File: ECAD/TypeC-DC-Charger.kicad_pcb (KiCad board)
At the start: 4 copper layers, 48 x 56 mm, 97 parts, among them CON1 XT60-PT-MALE, J1 USB_C_SOCKET_RA_SMD, Q1 CSD18543Q3A, Q2 CSD18543Q3A, Q3 CSD17551Q3A, Q4 CSD17551Q3A, Q5 CSD17579Q3A, Q6 CSD17579Q3A, Q7 CSD17579Q3A, Q8 BC857B, Q9 IRFR9024NTRPBF, SW1 2.54mm_3xSPST_SMD, U1 LM5175RHF, U2 TPS25741, U3 TPS2514

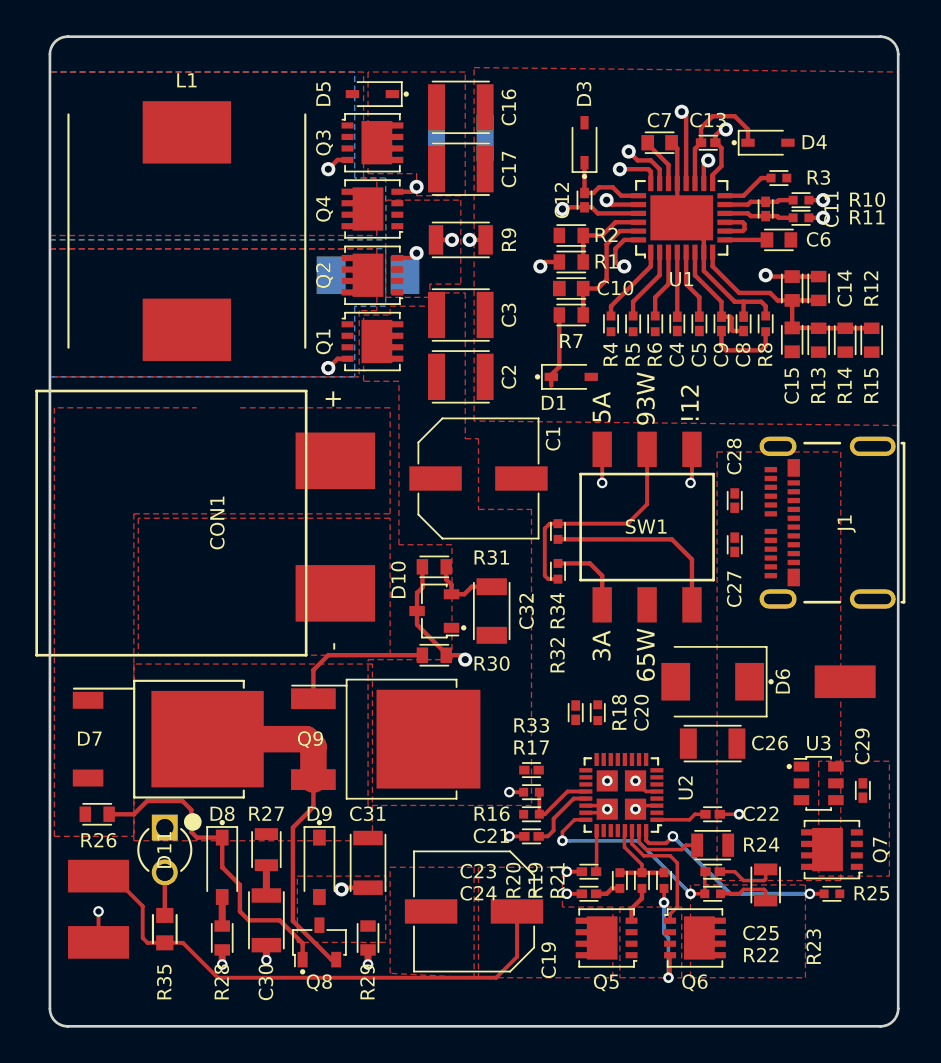
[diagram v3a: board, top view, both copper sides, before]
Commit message: Adding vias on thermal planes
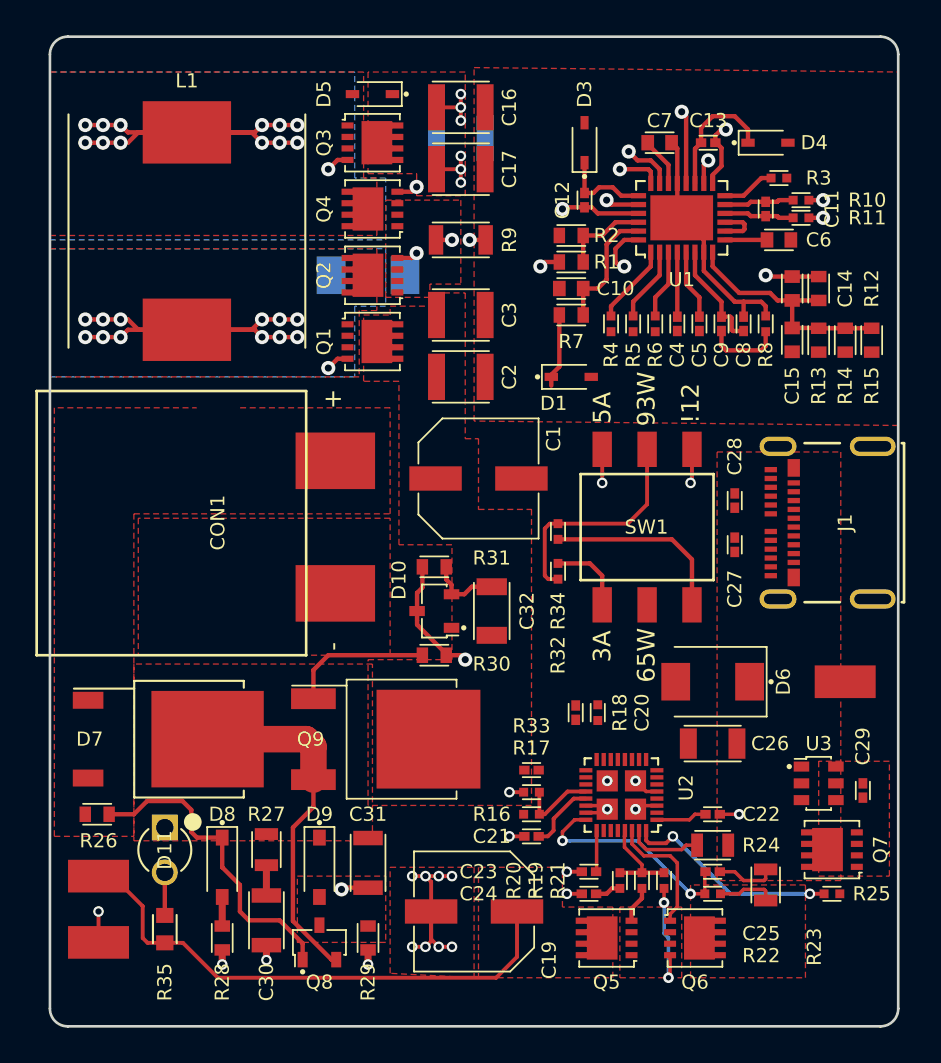
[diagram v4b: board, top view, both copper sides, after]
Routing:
- net SW2: track 3.82 -> 28.7 mm, vias 1 -> 13
- net SW1: track 4.49 -> 29.3 mm, vias 1 -> 13
- net GND: track 33.3 -> 43.5 mm, vias 17 -> 25
- net VARIABLE_DC: track 40.9 -> 46.6 mm, vias 2 -> 8
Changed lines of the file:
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@@
     (thickness 1)
     (drawings 15)
-    (tracks 353)
+    (tracks 442)
     (zones 0)
     (modules 97)
@@
   (segment (start 136.75 64.75) (end 136.75 65.845) (width 0.25) (layer F.Cu) (net 10))
   (segment (start 136 62.195) (end 136 64) (width 0.25) (layer F.Cu) (net 10))
+  (segment (start 123.25 54) (end 123.25 54.75) (width 0.22) (layer F.Cu) (net 11))
+  (via (at 123.25 54.75) (size 0.6) (drill 0.35) (layers F.Cu B.Cu) (net 11))
+  (segment (start 123.25 54) (end 123.25 53.25) (width 0.22) (layer F.Cu) (net 11))
+  (via (at 123.25 53.25) (size 0.6) (drill 0.35) (layers F.Cu B.Cu) (net 11))
+  (segment (start 121.875 54) (end 123.25 54) (width 0.22) (layer F.Cu) (net 11))
+  (via (at 123.25 54) (size 0.6) (drill 0.35) (layers F.Cu B.Cu) (net 11))
+  (segment (start 123.25 57.5) (end 123.25 56.75) (width 0.22) (layer F.Cu) (net 11))
+  (via (at 123.25 56.75) (size 0.6) (drill 0.35) (layers F.Cu B.Cu) (net 11))
+  (segment (start 123.25 57.5) (end 123.25 58.25) (width 0.22) (layer F.Cu) (net 11))
+  (via (at 123.25 58.25) (size 0.6) (drill 0.35) (layers F.Cu B.Cu) (net 11))
+  (segment (start 121.875 57.5) (end 123.25 57.5) (width 0.22) (layer F.Cu) (net 11))
+  (via (at 123.25 57.5) (size 0.6) (drill 0.35) (layers F.Cu B.Cu) (net 11))
   (segment (start 106.5 101.275) (end 107.525 101.275) (width 0.22) (layer F.Cu) (net 11))
   (segment (start 107.525 101.275) (end 109.5 103.25) (width 0.22) (layer F.Cu) (net 11))
@@
   (segment (start 136.5 58.305) (end 136.5 56.345) (width 0.25) (layer F.Cu) (net 18))
   (segment (start 136.5 56.345) (end 136.845 56) (width 0.25) (layer F.Cu) (net 18))
+  (segment (start 113 56) (end 114 56) (width 0.25) (layer F.Cu) (net 19))
+  (via (at 114 56) (size 0.8) (drill 0.4) (layers F.Cu B.Cu) (net 19))
+  (segment (start 112 56) (end 113 56) (width 0.25) (layer F.Cu) (net 19))
+  (via (at 113 56) (size 0.8) (drill 0.4) (layers F.Cu B.Cu) (net 19))
+  (segment (start 107.75 55.415) (end 111.415 55.415) (width 0.25) (layer F.Cu) (net 19))
+  (segment (start 111.415 55.415) (end 112 56) (width 0.25) (layer F.Cu) (net 19))
+  (via (at 112 56) (size 0.8) (drill 0.4) (layers F.Cu B.Cu) (net 19))
+  (segment (start 113 55) (end 114 55) (width 0.25) (layer F.Cu) (net 19))
+  (via (at 114 55) (size 0.8) (drill 0.4) (layers F.Cu B.Cu) (net 19))
+  (segment (start 112 55) (end 113 55) (width 0.25) (layer F.Cu) (net 19))
+  (via (at 113 55) (size 0.8) (drill 0.4) (layers F.Cu B.Cu) (net 19))
+  (segment (start 107.75 55.415) (end 111.585 55.415) (width 0.25) (layer F.Cu) (net 19))
+  (segment (start 111.585 55.415) (end 112 55) (width 0.25) (layer F.Cu) (net 19))
+  (via (at 112 55) (size 0.8) (drill 0.4) (layers F.Cu B.Cu) (net 19))
+  (segment (start 103 55) (end 102 55) (width 0.25) (layer F.Cu) (net 19))
+  (via (at 102 55) (size 0.8) (drill 0.4) (layers F.Cu B.Cu) (net 19))
+  (segment (start 104 55) (end 103 55) (width 0.25) (layer F.Cu) (net 19))
+  (via (at 103 55) (size 0.8) (drill 0.4) (layers F.Cu B.Cu) (net 19))
+  (segment (start 107.75 55.415) (end 104.415 55.415) (width 0.25) (layer F.Cu) (net 19))
+  (segment (start 104.415 55.415) (end 104 55) (width 0.25) (layer F.Cu) (net 19))
+  (via (at 104 55) (size 0.8) (drill 0.4) (layers F.Cu B.Cu) (net 19))
+  (segment (start 103 56) (end 102 56) (width 0.25) (layer F.Cu) (net 19))
+  (via (at 102 56) (size 0.8) (drill 0.4) (layers F.Cu B.Cu) (net 19))
+  (segment (start 104 56) (end 103 56) (width 0.25) (layer F.Cu) (net 19))
+  (via (at 103 56) (size 0.8) (drill 0.4) (layers F.Cu B.Cu) (net 19))
+  (segment (start 107.75 55.415) (end 105 55.415) (width 0.25) (layer F.Cu) (net 19))
+  (segment (start 105 55.415) (end 104.415 56) (width 0.25) (layer F.Cu) (net 19))
+  (segment (start 104.415 56) (end 104 56) (width 0.25) (layer F.Cu) (net 19))
+  (via (at 104 56) (size 0.8) (drill 0.4) (layers F.Cu B.Cu) (net 19))
   (segment (start 137.655 56) (end 137.655 55.595) (width 0.25) (layer F.Cu) (net 19))
   (segment (start 138 55.25) (end 138.25 55.25) (width 0.25) (layer F.Cu) (net 19))
@@
   (segment (start 128.37 69.13) (end 128.37 69.75) (width 0.25) (layer F.Cu) (net 28))
   (segment (start 128.825 65.75) (end 128.825 68.675) (width 0.25) (layer F.Cu) (net 28))
+  (segment (start 113 67) (end 114 67) (width 0.25) (layer F.Cu) (net 29))
+  (via (at 114 67) (size 0.8) (drill 0.4) (layers F.Cu B.Cu) (net 29))
+  (segment (start 112 67) (end 113 67) (width 0.25) (layer F.Cu) (net 29))
+  (via (at 113 67) (size 0.8) (drill 0.4) (layers F.Cu B.Cu) (net 29))
+  (segment (start 107.75 66.585) (end 111.585 66.585) (width 0.25) (layer F.Cu) (net 29))
+  (segment (start 111.585 66.585) (end 112 67) (width 0.25) (layer F.Cu) (net 29))
+  (via (at 112 67) (size 0.8) (drill 0.4) (layers F.Cu B.Cu) (net 29))
+  (segment (start 113 66) (end 114 66) (width 0.25) (layer F.Cu) (net 29))
+  (via (at 114 66) (size 0.8) (drill 0.4) (layers F.Cu B.Cu) (net 29))
+  (segment (start 112 66) (end 113 66) (width 0.25) (layer F.Cu) (net 29))
+  (via (at 113 66) (size 0.8) (drill 0.4) (layers F.Cu B.Cu) (net 29))
+  (segment (start 107.75 66.585) (end 111.415 66.585) (width 0.25) (layer F.Cu) (net 29))
+  (segment (start 111.415 66.585) (end 112 66) (width 0.25) (layer F.Cu) (net 29))
+  (via (at 112 66) (size 0.8) (drill 0.4) (layers F.Cu B.Cu) (net 29))
+  (via (at 102 66) (size 0.8) (drill 0.4) (layers F.Cu B.Cu) (net 29))
+  (segment (start 103 66) (end 102 66) (width 0.25) (layer F.Cu) (net 29))
+  (segment (start 104 66) (end 103 66) (width 0.25) (layer F.Cu) (net 29))
+  (via (at 103 66) (size 0.8) (drill 0.4) (layers F.Cu B.Cu) (net 29))
+  (segment (start 103 67) (end 102 67) (width 0.25) (layer F.Cu) (net 29))
+  (via (at 102 67) (size 0.8) (drill 0.4) (layers F.Cu B.Cu) (net 29))
+  (segment (start 104 67) (end 103 67) (width 0.25) (layer F.Cu) (net 29))
+  (via (at 103 67) (size 0.8) (drill 0.4) (layers F.Cu B.Cu) (net 29))
+  (segment (start 107.75 66.585) (end 105 66.585) (width 0.25) (layer F.Cu) (net 29))
+  (segment (start 105 66.585) (end 104.415 66) (width 0.25) (layer F.Cu) (net 29))
+  (segment (start 104.415 66) (end 104 66) (width 0.25) (layer F.Cu) (net 29))
+  (via (at 104 66) (size 0.8) (drill 0.4) (layers F.Cu B.Cu) (net 29))
+  (segment (start 107.75 66.585) (end 104.415 66.585) (width 0.25) (layer F.Cu) (net 29))
+  (segment (start 104.415 66.585) (end 104 67) (width 0.25) (layer F.Cu) (net 29))
+  (via (at 104 67) (size 0.8) (drill 0.4) (layers F.Cu B.Cu) (net 29))
   (segment (start 130.25 59.655) (end 129.095 59.655) (width 0.25) (layer F.Cu) (net 29))
   (segment (start 129.095 59.655) (end 129 59.75) (width 0.25) (layer F.Cu) (net 29))
@@
   (segment (start 138 65) (end 138 65.845) (width 0.25) (layer F.Cu) (net 65))
   (segment (start 136.5 62.195) (end 136.5 63.5) (width 0.25) (layer F.Cu) (net 65))
+  (segment (start 122 97.5) (end 122.75 97.5) (width 0.22) (layer F.Cu) (net 66))
+  (via (at 122.75 97.5) (size 0.6) (drill 0.35) (layers F.Cu B.Cu) (net 66))
+  (via (at 122 97.5) (size 0.6) (drill 0.35) (layers F.Cu B.Cu) (net 66))
+  (segment (start 121.25 97.5) (end 122 97.5) (width 0.22) (layer F.Cu) (net 66))
+  (segment (start 121.25 97.5) (end 120.5 97.5) (width 0.22) (layer F.Cu) (net 66))
+  (via (at 120.5 97.5) (size 0.6) (drill 0.35) (layers F.Cu B.Cu) (net 66))
+  (segment (start 121.57 99.5) (end 121.57 97.82) (width 0.22) (layer F.Cu) (net 66))
+  (segment (start 121.57 97.82) (end 121.25 97.5) (width 0.22) (layer F.Cu) (net 66))
+  (via (at 121.25 97.5) (size 0.6) (drill 0.35) (layers F.Cu B.Cu) (net 66))
+  (segment (start 121.25 101.5) (end 120.5 101.5) (width 0.22) (layer F.Cu) (net 66))
+  (via (at 120.5 101.5) (size 0.6) (drill 0.35) (layers F.Cu B.Cu) (net 66))
+  (segment (start 122 101.5) (end 122.75 101.5) (width 0.22) (layer F.Cu) (net 66))
+  (via (at 122.75 101.5) (size 0.6) (drill 0.35) (layers F.Cu B.Cu) (net 66))
+  (segment (start 121.57 99.5) (end 121.57 101.07) (width 0.22) (layer F.Cu) (net 66))
+  (segment (start 121.57 101.07) (end 122 101.5) (width 0.22) (layer F.Cu) (net 66))
+  (via (at 122 101.5) (size 0.6) (drill 0.35) (layers F.Cu B.Cu) (net 66))
+  (segment (start 121.57 99.5) (end 121.57 101.18) (width 0.22) (layer F.Cu) (net 66))
+  (segment (start 121.57 101.18) (end 121.25 101.5) (width 0.22) (layer F.Cu) (net 66))
+  (via (at 121.25 101.5) (size 0.6) (drill 0.35) (layers F.Cu B.Cu) (net 66))
   (segment (start 102.75 101.25) (end 102.75 99.5) (width 0.22) (layer F.Cu) (net 66))
   (via (at 102.75 99.5) (size 0.6) (drill 0.35) (layers F.Cu B.Cu) (net 66))

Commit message: Vias and power supply signal routing
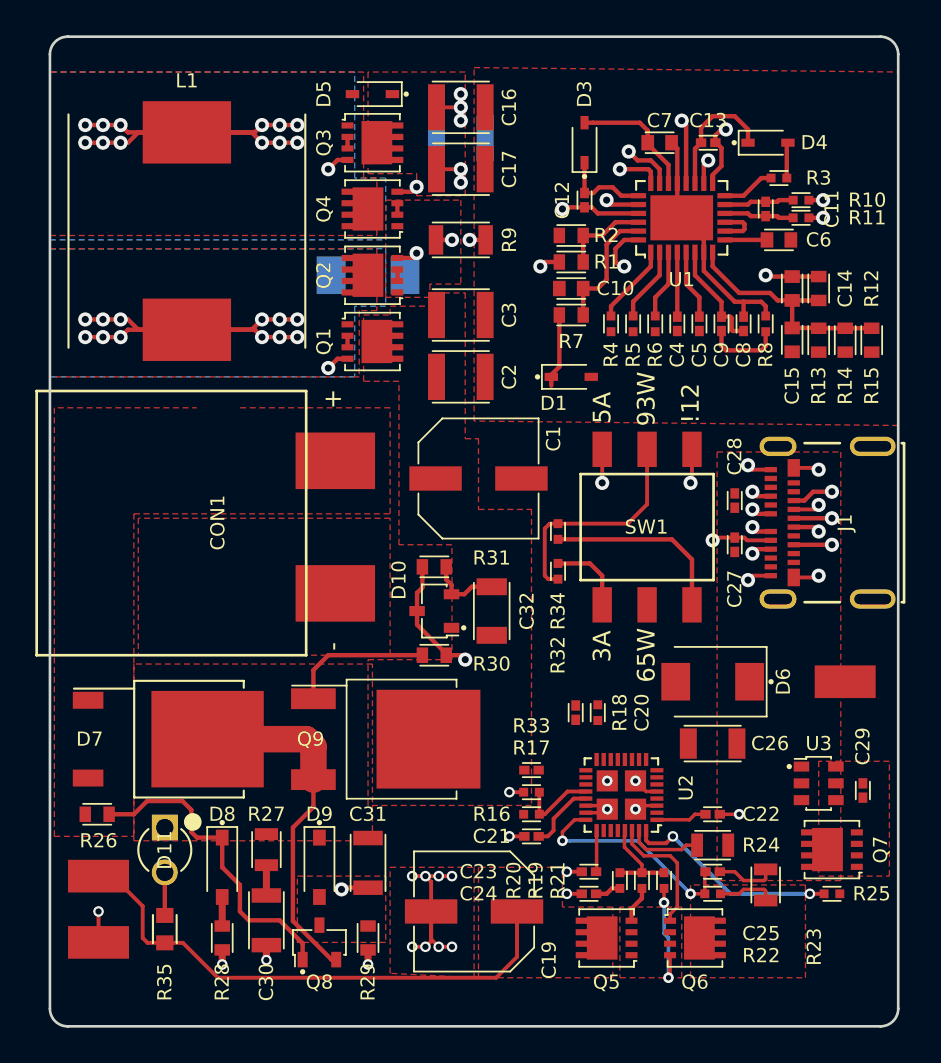
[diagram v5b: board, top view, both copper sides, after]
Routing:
- net SW2: track 28.7 -> 55.9 mm
- net GND: track 43.5 -> 69.9 mm, vias 25 -> 29
- net HDRV2: track 2.72 -> 28.2 mm
- net RCS: track 1.71 -> 25.5 mm
- net HDRV1: track 3.22 -> 24.7 mm
- net SW1: track 29.3 -> 49.2 mm
- net LDRV2: track 5.36 -> 22.1 mm
- net LDRV1: track 3.68 -> 18.0 mm
- net VARIABLE_DC: track 46.6 -> 56.1 mm, vias 8 -> 7
- net VBUS: track 3.38 -> 10.2 mm, vias 0 -> 4
- net /Power Supply/VCC: track 2.79 -> 9.26 mm
- net VIN: track 4.04 -> 8.79 mm
- net CC1: track 0.00 -> 3.42 mm, vias 0 -> 1
- net D+: track 0.00 -> 3.30 mm, vias 0 -> 2
- net D-: track 0.00 -> 2.66 mm, vias 0 -> 2
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
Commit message: Routing signals and more power planes and misc
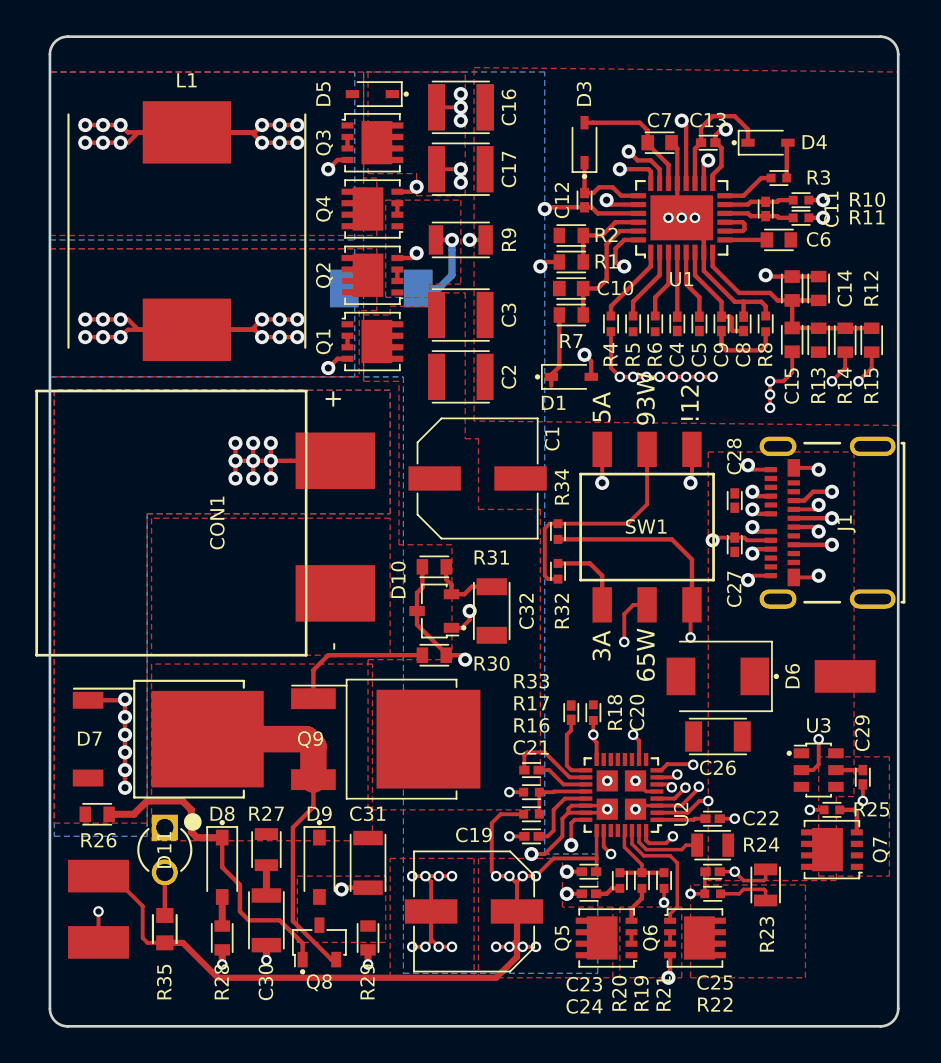
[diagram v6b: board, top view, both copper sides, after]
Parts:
- moved R25 4.75 mm to (144.2, 93.8)
- moved C18 1.75 mm to (123.2, 54.0)
- moved D2 1.06 mm to (118.8, 64.2)
- moved C29 0.75 mm to (146.0, 91.9)
- moved U3 0.75 mm to (143.5, 91.5)
- moved C26 0.50 mm to (137.8, 89.6)
- moved D6 0.42 mm to (137.8, 86.2)
- moved TEST3 0.30 mm to (145.0, 86.2)
- moved C20 0.25 mm to (129.5, 88.2)
- moved C22 0.25 mm to (137.5, 94.2)
- moved R18 0.25 mm to (130.8, 88.2)
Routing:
- net GND: track 69.9 -> 97.3 mm, vias 29 -> 48
- net VARIABLE_DC: track 56.1 -> 76.7 mm, vias 7 -> 15
- net /Connectors/RAW_BATT: track 0.00 -> 18.8 mm, vias 0 -> 15
- net Net-(C31-Pad2): track 8.53 -> 26.9 mm
- net /USBC Controller/EN12V: track 10.6 -> 22.2 mm, vias 0 -> 2
- net /USBC Controller/PSEL: track 0.00 -> 11.3 mm, vias 0 -> 2
- net VBUS: track 10.2 -> 19.1 mm, vias 4 -> 6
- net /USBC Controller/DVDD: track 13.0 -> 21.8 mm
- net RCS: track 25.5 -> 29.7 mm
- net CTRL2: track 0.00 -> 4.17 mm, vias 0 -> 2
- net CTRL1: track 0.00 -> 3.18 mm, vias 0 -> 2
- net CC1: track 3.42 -> 6.60 mm, vias 1 -> 2
- net Net-(R33-Pad2): track 0.00 -> 3.01 mm
- net Net-(Q7-Pad1): track 0.00 -> 2.15 mm
- net CC2: track 1.51 -> 3.39 mm, vias 1 -> 2
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- added copper zone on B.Cu, net /Connectors/RAW_BATT
- added copper zone on B.Cu, net VARIABLE_DC
